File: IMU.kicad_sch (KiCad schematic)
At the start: 1 part, among them U3 LSM6DSOXTR

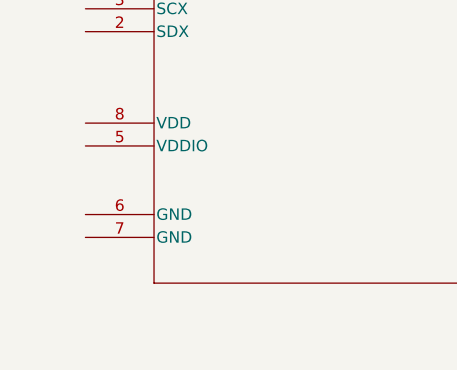
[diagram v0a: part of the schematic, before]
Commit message: Finished power section.
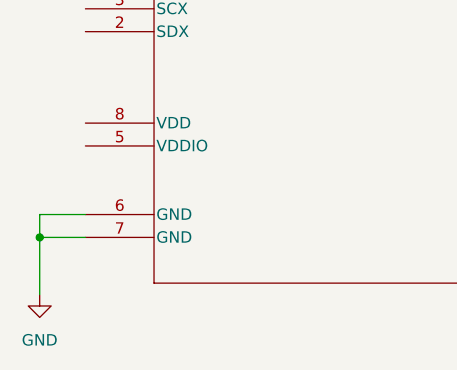
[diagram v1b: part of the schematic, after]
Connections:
- net GND: now reaches U3.6 (GND)
- net GND: now also U3.7 (GND)
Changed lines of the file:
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@@
 (kicad_sch
-	(version 20231120)
+	(version 20250114)
 	(generator "eeschema")
-	(generator_version "8.0")
+	(generator_version "9.0")
 	(paper "A4")
+	(junction
+		(at 110.49 113.03)
+		(diameter 0)
+		(color 0 0 0 0)
+	)
+	(wire
+		(pts
+			(xy 110.49 110.49) (xy 110.49 113.03)
+		)
+		(stroke
+			(width 0)
+			(type default)
+		)
+	)
+	(wire
+		(pts
+			(xy 115.57 113.03) (xy 110.49 113.03)
+		)
+		(stroke
+			(width 0)
+			(type default)
+		)
+	)
+	(wire
+		(pts
+			(xy 115.57 110.49) (xy 110.49 110.49)
+		)
+		(stroke
+			(width 0)
+			(type default)
+		)
+	)
+	(wire
+		(pts
+			(xy 110.49 113.03) (xy 110.49 119.38)
+		)
+		(stroke
+			(width 0)
+			(type default)
+		)
+	)
 	(symbol
 		(lib_id "Hourglass_symbol_library:LSM6DSOXTR")
@@
 					(unit 1)
 				)
+			)
+		)
+	)
+	(symbol
+		(lib_id "power:GND")
+		(at 110.49 119.38 0)
+		(unit 1)
+		(exclude_from_sim no)
+		(in_bom yes)
+		(on_board yes)
+		(dnp no)
+		(fields_autoplaced yes)
+		(property "Reference" "#PWR2"
+			(at 110.49 125.73 0)
+			(effects
+				(font
+					(size 1.27 1.27)
+				)
+				(hide yes)
+			)
+		)
+		(property "Value" "GND"
+			(at 110.49 124.46 0)
+			(effects
+				(font
+					(size 1.27 1.27)
+				)
+			)
+		)
+		(property "Footprint" ""
+			(at 110.49 119.38 0)
+			(effects
+				(font
+					(size 1.27 1.27)
+				)
+				(hide yes)
+			)
+		)
+		(property "Datasheet" ""
+			(at 110.49 119.38 0)
+			(effects
+				(font
+					(size 1.27 1.27)
+				)
+				(hide yes)
+			)
+		)
+		(property "Description" "Power symbol creates a global label with name \"GND\" , ground"
+			(at 110.49 119.38 0)
+			(effects
+				(font
+					(size 1.27 1.27)
+				)
+				(hide yes)
+			)
+		)
+		(pin "1"
+		)
+		(instances
+			(project ""
+				(path "/a75630d2-15a7-42bc-8ce0-7846cbd1da6b/e8095abd-2da6-4096-a23d-04399ef236ae"
+					(reference "#PWR2")
+					(unit 1)
+				)

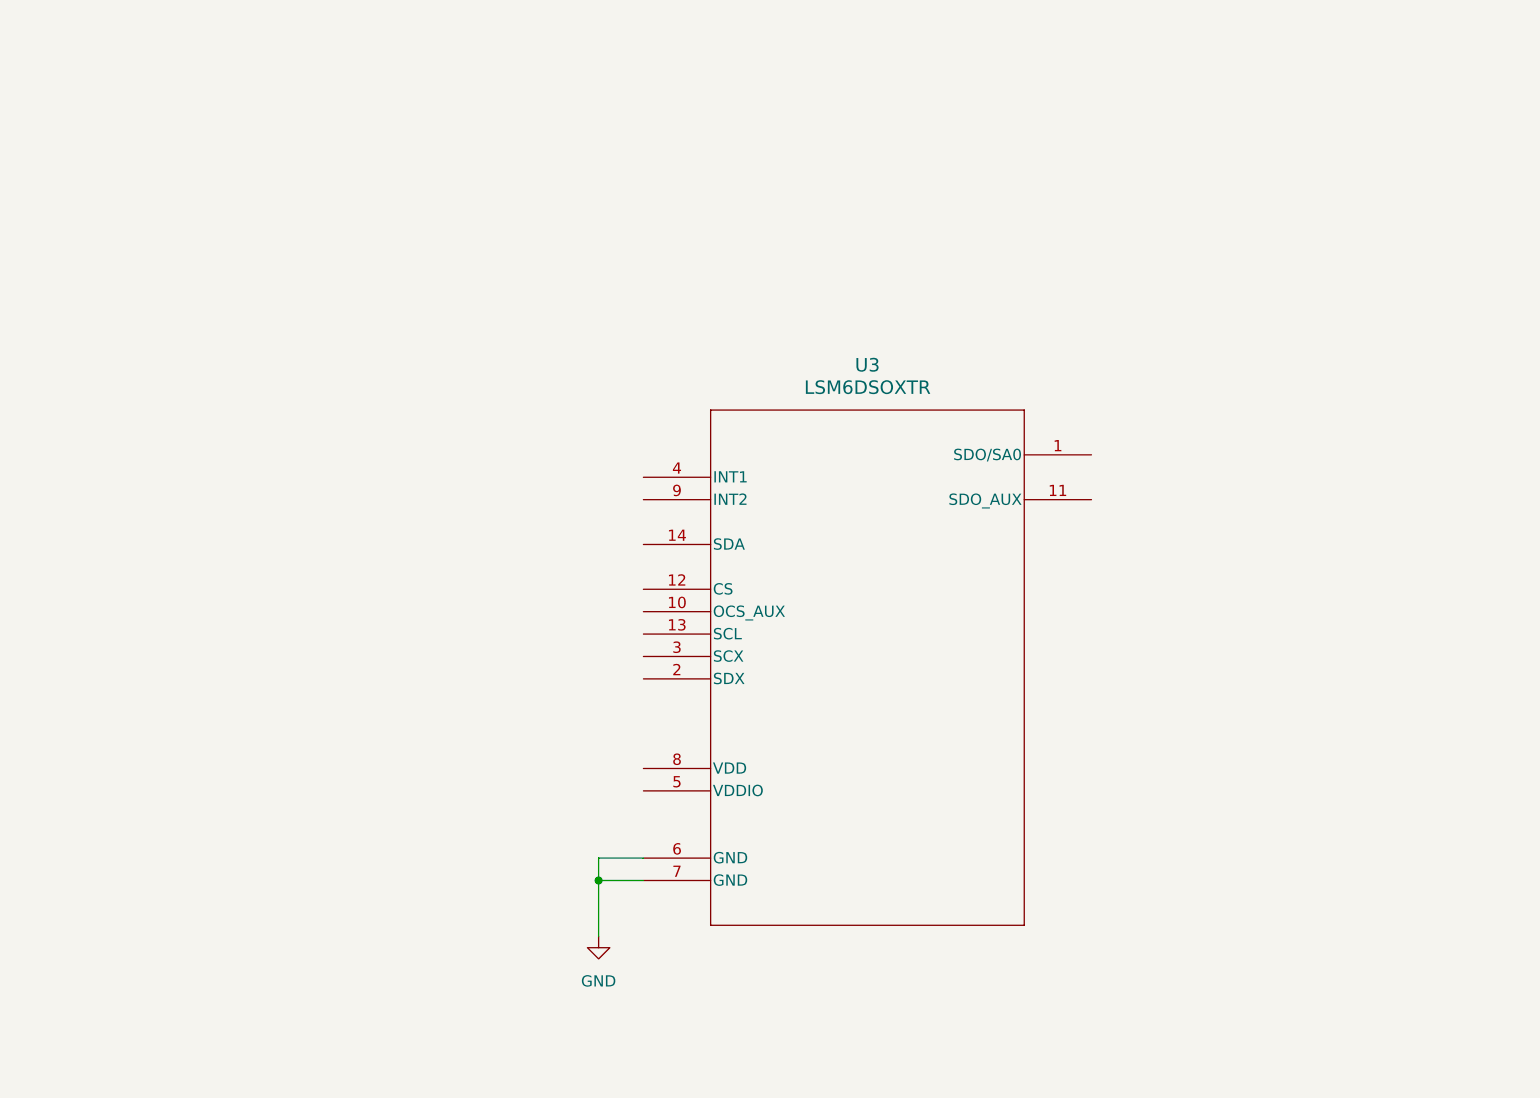
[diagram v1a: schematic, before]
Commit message: Finished LSM6DSOX schematic
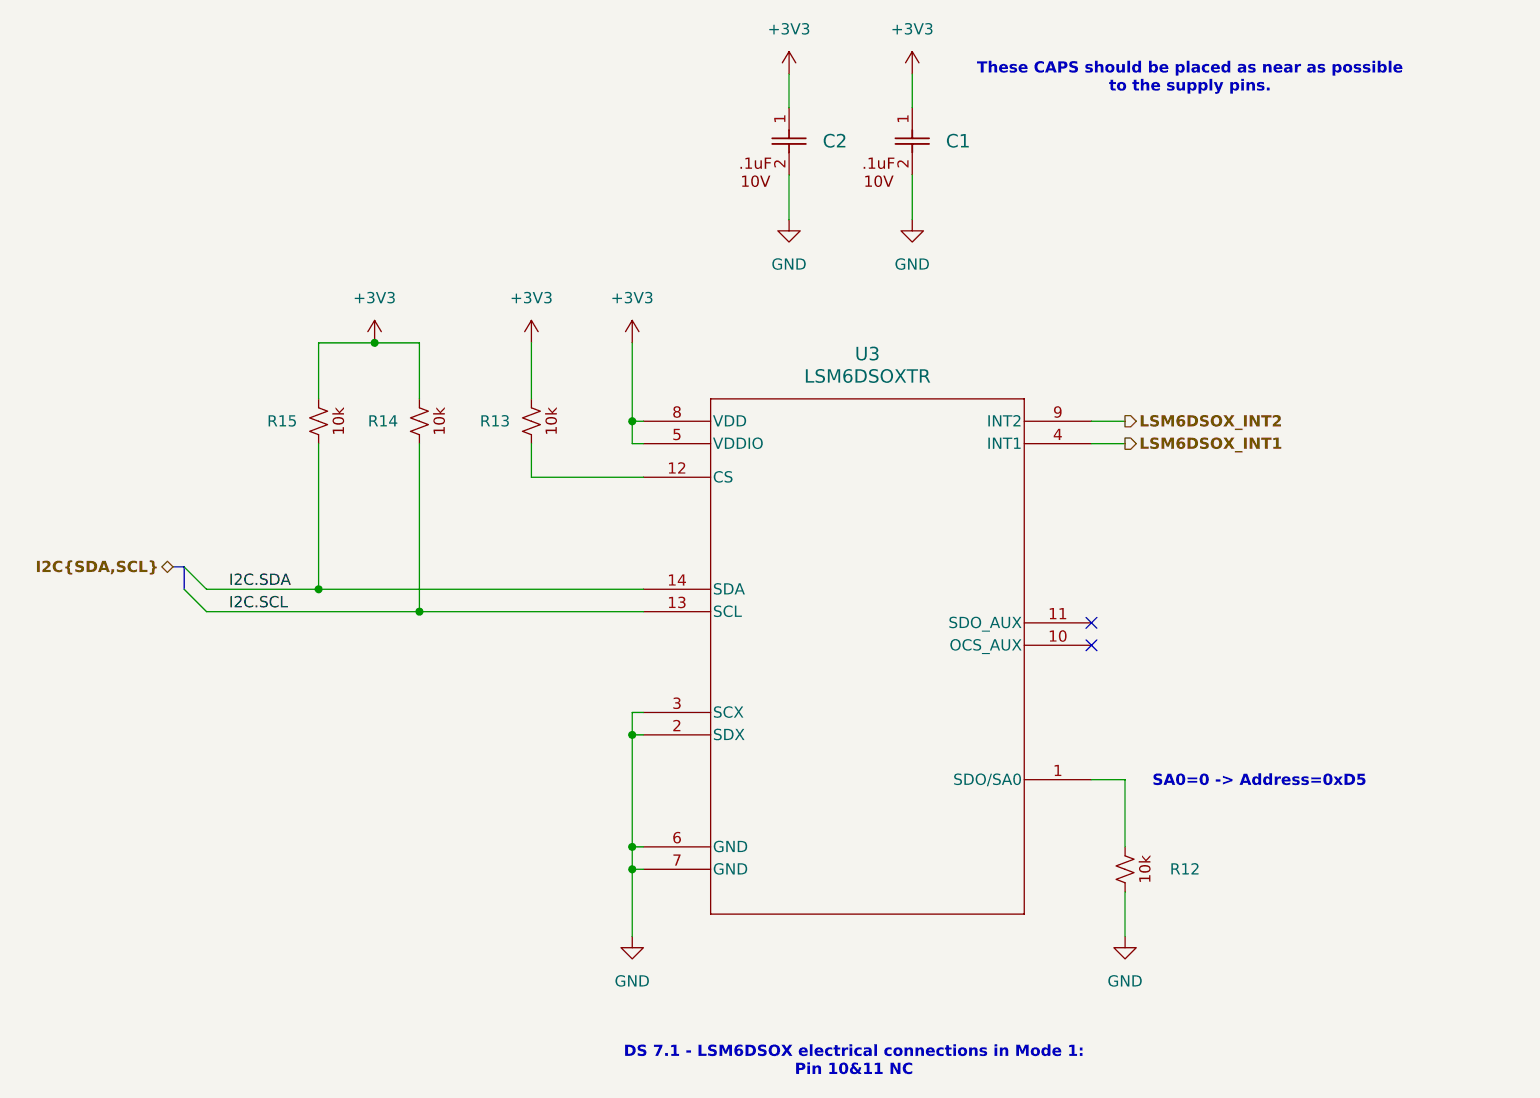
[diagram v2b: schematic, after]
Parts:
- added C1, C2: CC0402KRX7R6BB104, Hourglass_footprint_library:YAG_CC0402_YAG, symbol Hourglass_symbol_library:CC0402KRX7R6BB104
- added R12, R13, R14, R15: RMCF0805FT10K0, Hourglass_footprint_library:RMCF0805FT10K0, symbol Hourglass_symbol_library:RMCF0805FT10K0
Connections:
- net GND: now also U3.2 (SDX), U3.3 (SCX), C1.2, C2.2, R12.
- net at U3.1 (SDO/SA0): now also R12.
- net at U3.12 (CS): now also R13.
- net I2C.SCL: now reaches U3.13 (SCL)
- net I2C.SCL: now also R14.
- net I2C.SDA: now reaches U3.14 (SDA)
- net I2C.SDA: now also R15.
- net LSM6DSOX_INT1: now reaches U3.4 (INT1)
- net +3V3: now reaches U3.5 (VDDIO)
- net +3V3: now also U3.8 (VDD), C1.1, C2.1, R13., R14., R15.
- net LSM6DSOX_INT2: now reaches U3.9 (INT2)
- no-connect marks 0 -> 2
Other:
- note added: "DS 7.1 - LSM6DSOX electrical connections in Mode 1: Pin 10&11 NC"
- note added: "SA0=0 -> Address=0xD5"
- note added: "These CAPS should be placed as near as possible to the supply pins."
- moved on the sheet: U3

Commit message: Initial complete implementation of LEDS.
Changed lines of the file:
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@@
 		)
 	)
-	(hierarchical_label "I2C{SDA,SCL}"
+	(hierarchical_label "I2C{SDA SCL}"
 		(shape bidirectional)
 		(at 62.23 77.47 180)
@@
 		(dnp no)
 		(fields_autoplaced yes)
-		(property "Reference" "#PWR031"
+		(property "Reference" "#PWR31"
 			(at 146.05 44.45 0)
 			(effects
@@
 			(project ""
 				(path "/a75630d2-15a7-42bc-8ce0-7846cbd1da6b/e8095abd-2da6-4096-a23d-04399ef236ae"
-					(reference "#PWR031")
+					(reference "#PWR31")
 					(unit 1)
 				)
@@
 		(on_board yes)
 		(dnp no)
-		(property "Reference" "#PWR029"
+		(property "Reference" "#PWR29"
 			(at 146.05 25.4 0)
 			(effects
@@
 			(project "Hourglass_PCBA"
 				(path "/a75630d2-15a7-42bc-8ce0-7846cbd1da6b/e8095abd-2da6-4096-a23d-04399ef236ae"
-					(reference "#PWR029")
+					(reference "#PWR29")
 					(unit 1)
 				)
@@
 		(dnp no)
 		(fields_autoplaced yes)
-		(property "Reference" "#PWR030"
+		(property "Reference" "#PWR30"
 			(at 132.08 44.45 0)
 			(effects
@@
 			(project ""
 				(path "/a75630d2-15a7-42bc-8ce0-7846cbd1da6b/e8095abd-2da6-4096-a23d-04399ef236ae"
-					(reference "#PWR030")
+					(reference "#PWR30")
 					(unit 1)
 				)
@@
 		(on_board yes)
 		(dnp no)
-		(property "Reference" "#PWR027"
+		(property "Reference" "#PWR27"
 			(at 132.08 25.4 0)
 			(effects
@@
 			(project "Hourglass_PCBA"
 				(path "/a75630d2-15a7-42bc-8ce0-7846cbd1da6b/e8095abd-2da6-4096-a23d-04399ef236ae"
-					(reference "#PWR027")
-					(unit 1)
-				)
+					(reference "#PWR27")
+					(unit 1)
+				)

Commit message: First complete schematic with TPs.
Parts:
- added TP31, TP32, TP33: TestPoint, TestPoint:TestPoint_Pad_D1.0mm, symbol Connector:TestPoint
- renumbered C2 to C11, C1 to C12, R15 to R2, R14 to R3, R13 to R4, R12 to R5
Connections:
- net LSM6DSOX_INT1: now also TP32.1
- net LSM6DSOX_INT2: now also TP31.1
- net at R4., U3.12 (CS): now also TP33.1

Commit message: Addressed DRC warnings and errors.
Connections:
- net +3V3: now also R2.2, R3.2, R4.2; no longer R2., R3., R4.
- net GND: now also R5.1; no longer R5.
- net I2C.SCL: now also R3.1; no longer R3.
- net I2C.SDA: now also R2.1; no longer R2.
- net at TP33.1, U3.12 (CS): now also R4.1; no longer R4.
- net at U3.1 (SDO/SA0): now also R5.2; no longer R5.
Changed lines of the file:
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@@
 		(on_board yes)
 		(dnp no)
-		(property "Reference" "#PWR020"
+		(property "Reference" "#PWR20"
 			(at 85.09 55.88 0)
 			(effects
@@
 			(project "Hourglass_PCBA"
 				(path "/a75630d2-15a7-42bc-8ce0-7846cbd1da6b/e8095abd-2da6-4096-a23d-04399ef236ae"
-					(reference "#PWR020")
-					(unit 1)
-				)
-			)
-		)
-	)
-	(symbol
-		(lib_name "RMCF0805FT10K0_3")
+					(reference "#PWR20")
+					(unit 1)
+				)
+			)
+		)
+	)
+	(symbol
 		(lib_id "Hourglass_symbol_library:RMCF0805FT10K0")
 		(at 90.17 60.96 90)
@@
 			)
 		)
-		(pin ""
-		)
-		(pin ""
+		(pin "1"
+		)
+		(pin "2"
 		)
 		(instances
@@
 		(on_board yes)
 		(dnp no)
-		(property "Reference" "#PWR021"
+		(property "Reference" "#PWR21"
 			(at 102.87 55.88 0)
 			(effects
@@
 			(project "Hourglass_PCBA"
 				(path "/a75630d2-15a7-42bc-8ce0-7846cbd1da6b/e8095abd-2da6-4096-a23d-04399ef236ae"
-					(reference "#PWR021")
+					(reference "#PWR21")
 					(unit 1)
 				)
@@
 		(dnp no)
 		(fields_autoplaced yes)
-		(property "Reference" "#PWR019"
+		(property "Reference" "#PWR19"
 			(at 146.05 44.45 0)
 			(effects
@@
 			(project ""
 				(path "/a75630d2-15a7-42bc-8ce0-7846cbd1da6b/e8095abd-2da6-4096-a23d-04399ef236ae"
-					(reference "#PWR019")
+					(reference "#PWR19")
 					(unit 1)
 				)
@@
 		(on_board yes)
 		(dnp no)
-		(property "Reference" "#PWR022"
+		(property "Reference" "#PWR22"
 			(at 114.3 55.88 0)
 			(effects
@@
 			(project ""
 				(path "/a75630d2-15a7-42bc-8ce0-7846cbd1da6b/e8095abd-2da6-4096-a23d-04399ef236ae"
-					(reference "#PWR022")
+					(reference "#PWR22")
 					(unit 1)
 				)
@@
 			)
 		)
-		(pin ""
-		)
-		(pin ""
+		(pin "1"
+		)
+		(pin "2"
 		)
 		(instances
@@
 		(on_board yes)
 		(dnp no)
-		(property "Reference" "#PWR017"
+		(property "Reference" "#PWR17"
 			(at 146.05 25.4 0)
 			(effects
@@
 			(project "Hourglass_PCBA"
 				(path "/a75630d2-15a7-42bc-8ce0-7846cbd1da6b/e8095abd-2da6-4096-a23d-04399ef236ae"
-					(reference "#PWR017")
+					(reference "#PWR17")
 					(unit 1)
 				)
@@
 		(dnp no)
 		(fields_autoplaced yes)
-		(property "Reference" "#PWR018"
+		(property "Reference" "#PWR18"
 			(at 132.08 44.45 0)
 			(effects
@@
 			(project ""
 				(path "/a75630d2-15a7-42bc-8ce0-7846cbd1da6b/e8095abd-2da6-4096-a23d-04399ef236ae"
-					(reference "#PWR018")
+					(reference "#PWR18")
 					(unit 1)
 				)
@@
 		(on_board yes)
 		(dnp no)
-		(property "Reference" "#PWR016"
+		(property "Reference" "#PWR16"
 			(at 132.08 25.4 0)
 			(effects
@@
 			(project "Hourglass_PCBA"
 				(path "/a75630d2-15a7-42bc-8ce0-7846cbd1da6b/e8095abd-2da6-4096-a23d-04399ef236ae"
-					(reference "#PWR016")
+					(reference "#PWR16")
 					(unit 1)
 				)
@@
 		(dnp no)
 		(fields_autoplaced yes)
-		(property "Reference" "#PWR024"
+		(property "Reference" "#PWR24"
 			(at 170.18 125.73 0)
 			(effects
@@
 			(project "Hourglass_PCBA"
 				(path "/a75630d2-15a7-42bc-8ce0-7846cbd1da6b/e8095abd-2da6-4096-a23d-04399ef236ae"
-					(reference "#PWR024")
+					(reference "#PWR24")
 					(unit 1)
 				)
@@
 			)
 		)
-		(property "Datasheet" "LSM6DSOXTR"
+		(property "Datasheet" "https://www.st.com/resource/en/datasheet/lsm6dsox.pdf"
 			(at 129.032 121.412 0)
 			(effects
@@
 		(dnp no)
 		(fields_autoplaced yes)
-		(property "Reference" "#PWR023"
+		(property "Reference" "#PWR23"
 			(at 114.3 125.73 0)
 			(effects
@@
 			(project ""
 				(path "/a75630d2-15a7-42bc-8ce0-7846cbd1da6b/e8095abd-2da6-4096-a23d-04399ef236ae"
-					(reference "#PWR023")
-					(unit 1)
-				)
-			)
-		)
-	)
-	(symbol
-		(lib_name "RMCF0805FT10K0_1")
+					(reference "#PWR23")
+					(unit 1)
+				)
+			)
+		)
+	)
+	(symbol
 		(lib_id "Hourglass_symbol_library:RMCF0805FT10K0")
 		(at 78.74 60.96 90)
@@
 			)
 		)
-		(pin ""
-		)
-		(pin ""
+		(pin "1"
+		)
+		(pin "2"
 		)
 		(instances
@@
 	)
 	(symbol
-		(lib_name "RMCF0805FT10K0_2")
 		(lib_id "Hourglass_symbol_library:RMCF0805FT10K0")
 		(at 170.18 111.76 90)
@@
 			)
 		)
-		(pin ""
-		)
-		(pin ""
-		)
-		(instances
+		(pin "1"
+		)
+		(pin "2"
+		)
+		(instances

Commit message: Changed PUs for I2C and added TPs.
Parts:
- removed R2, R3: RMCF0805FT10K0, Hourglass_footprint_library:RMCF0805FT10K0, symbol Hourglass_symbol_library:RMCF0805FT10K0
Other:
- moved on the sheet: TP31, TP32

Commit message: Updated addressing comment for LSM6DSOXTR and added ref image.
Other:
- note added: "SA0=0 -> Address=0x6A"
- note removed: "SA0=0 -> Address=0xD5"

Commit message: Re-annotated entire schematic.
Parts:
- renumbered R4 to R5, R5 to R6, TP31 to TP34, TP32 to TP35, TP33 to TP36
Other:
- title: (none) -> Hourglass
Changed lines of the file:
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@@
 	(generator_version "9.0")
 	(paper "A4")
+	(title_block
+		(title "Hourglass")
+		(date "2025-04-23")
+		(rev "01")
+	)
 	(text "DS 7.1 - LSM6DSOX electrical connections in Mode 1:\nPin 10&11 NC\n"
 		(exclude_from_sim yes)
@@
 		(on_board yes)
 		(dnp no)
-		(property "Reference" "#PWR21"
+		(property "Reference" "#PWR023"
 			(at 102.87 55.88 0)
 			(effects
@@
 			(project "Hourglass_PCBA"
 				(path "/a75630d2-15a7-42bc-8ce0-7846cbd1da6b/e8095abd-2da6-4096-a23d-04399ef236ae"
-					(reference "#PWR21")
+					(reference "#PWR023")
 					(unit 1)
 				)
@@
 		(dnp no)
 		(fields_autoplaced yes)
-		(property "Reference" "#PWR19"
+		(property "Reference" "#PWR022"
 			(at 146.05 44.45 0)
 			(effects
@@
 			(project ""
 				(path "/a75630d2-15a7-42bc-8ce0-7846cbd1da6b/e8095abd-2da6-4096-a23d-04399ef236ae"
-					(reference "#PWR19")
+					(reference "#PWR022")
 					(unit 1)
 				)
@@
 		(on_board yes)
 		(dnp no)
-		(property "Reference" "#PWR22"
+		(property "Reference" "#PWR024"
 			(at 114.3 55.88 0)
 			(effects
@@
 			(project ""
 				(path "/a75630d2-15a7-42bc-8ce0-7846cbd1da6b/e8095abd-2da6-4096-a23d-04399ef236ae"
-					(reference "#PWR22")
+					(reference "#PWR024")
 					(unit 1)
 				)
@@
 		(on_board yes)
 		(dnp no)
-		(property "Reference" "R4"
+		(property "Reference" "R5"
 			(at 97.028 60.9598 90)
 			(effects
@@
 			(project ""
 				(path "/a75630d2-15a7-42bc-8ce0-7846cbd1da6b/e8095abd-2da6-4096-a23d-04399ef236ae"
-					(reference "R4")
+					(reference "R5")
 					(unit 1)
 				)
@@
 		(on_board yes)
 		(dnp no)
-		(property "Reference" "#PWR17"
+		(property "Reference" "#PWR020"
 			(at 146.05 25.4 0)
 			(effects
@@
 			(project "Hourglass_PCBA"
 				(path "/a75630d2-15a7-42bc-8ce0-7846cbd1da6b/e8095abd-2da6-4096-a23d-04399ef236ae"
-					(reference "#PWR17")
+					(reference "#PWR020")
 					(unit 1)
 				)
@@
 		(on_board yes)
 		(dnp no)
-		(property "Reference" "TP31"
+		(property "Reference" "TP34"
 			(at 167.64 53.5939 90)
 			(effects
@@
 			(project ""
 				(path "/a75630d2-15a7-42bc-8ce0-7846cbd1da6b/e8095abd-2da6-4096-a23d-04399ef236ae"
-					(reference "TP31")
+					(reference "TP34")
 					(unit 1)
 				)
@@
 		(on_board yes)
 		(dnp no)
-		(property "Reference" "TP32"
+		(property "Reference" "TP35"
 			(at 172.72 53.8479 90)
 			(effects
@@
 			(project "Hourglass_PCBA"
 				(path "/a75630d2-15a7-42bc-8ce0-7846cbd1da6b/e8095abd-2da6-4096-a23d-04399ef236ae"
-					(reference "TP32")
+					(reference "TP35")
 					(unit 1)
 				)
@@
 		(dnp no)
 		(fields_autoplaced yes)
-		(property "Reference" "#PWR18"
+		(property "Reference" "#PWR021"
 			(at 132.08 44.45 0)
 			(effects
@@
 			(project ""
 				(path "/a75630d2-15a7-42bc-8ce0-7846cbd1da6b/e8095abd-2da6-4096-a23d-04399ef236ae"
-					(reference "#PWR18")
+					(reference "#PWR021")
 					(unit 1)
 				)
@@
 		(on_board yes)
 		(dnp no)
-		(property "Reference" "#PWR16"
+		(property "Reference" "#PWR019"
 			(at 132.08 25.4 0)
 			(effects
@@
 			(project "Hourglass_PCBA"
 				(path "/a75630d2-15a7-42bc-8ce0-7846cbd1da6b/e8095abd-2da6-4096-a23d-04399ef236ae"
-					(reference "#PWR16")
+					(reference "#PWR019")
 					(unit 1)
 				)
@@
 		(dnp no)
 		(fields_autoplaced yes)
-		(property "Reference" "#PWR24"
+		(property "Reference" "#PWR026"
 			(at 170.18 125.73 0)
 			(effects
@@
 			(project "Hourglass_PCBA"
 				(path "/a75630d2-15a7-42bc-8ce0-7846cbd1da6b/e8095abd-2da6-4096-a23d-04399ef236ae"
-					(reference "#PWR24")
+					(reference "#PWR026")
 					(unit 1)
 				)
@@
 		(dnp no)
 		(fields_autoplaced yes)
-		(property "Reference" "#PWR23"
+		(property "Reference" "#PWR025"
 			(at 114.3 125.73 0)
 			(effects
@@
 			(project ""
 				(path "/a75630d2-15a7-42bc-8ce0-7846cbd1da6b/e8095abd-2da6-4096-a23d-04399ef236ae"
-					(reference "#PWR23")
+					(reference "#PWR025")
 					(unit 1)
 				)
@@
 		(on_board yes)
 		(dnp no)
-		(property "Reference" "TP33"
+		(property "Reference" "TP36"
 			(at 96.266 67.31 90)
 			(effects
@@
 			(project "Hourglass_PCBA"
 				(path "/a75630d2-15a7-42bc-8ce0-7846cbd1da6b/e8095abd-2da6-4096-a23d-04399ef236ae"
-					(reference "TP33")
+					(reference "TP36")
 					(unit 1)
 				)
@@
 		(dnp no)
 		(fields_autoplaced yes)
-		(property "Reference" "R5"
+		(property "Reference" "R6"
 			(at 175.26 111.7598 90)
 			(effects
@@
 			(project ""
 				(path "/a75630d2-15a7-42bc-8ce0-7846cbd1da6b/e8095abd-2da6-4096-a23d-04399ef236ae"
-					(reference "R5")
+					(reference "R6")
 					(unit 1)
 				)
